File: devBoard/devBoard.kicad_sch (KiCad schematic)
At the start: 1 part, among them U1 ESP32-S3-MINI-1

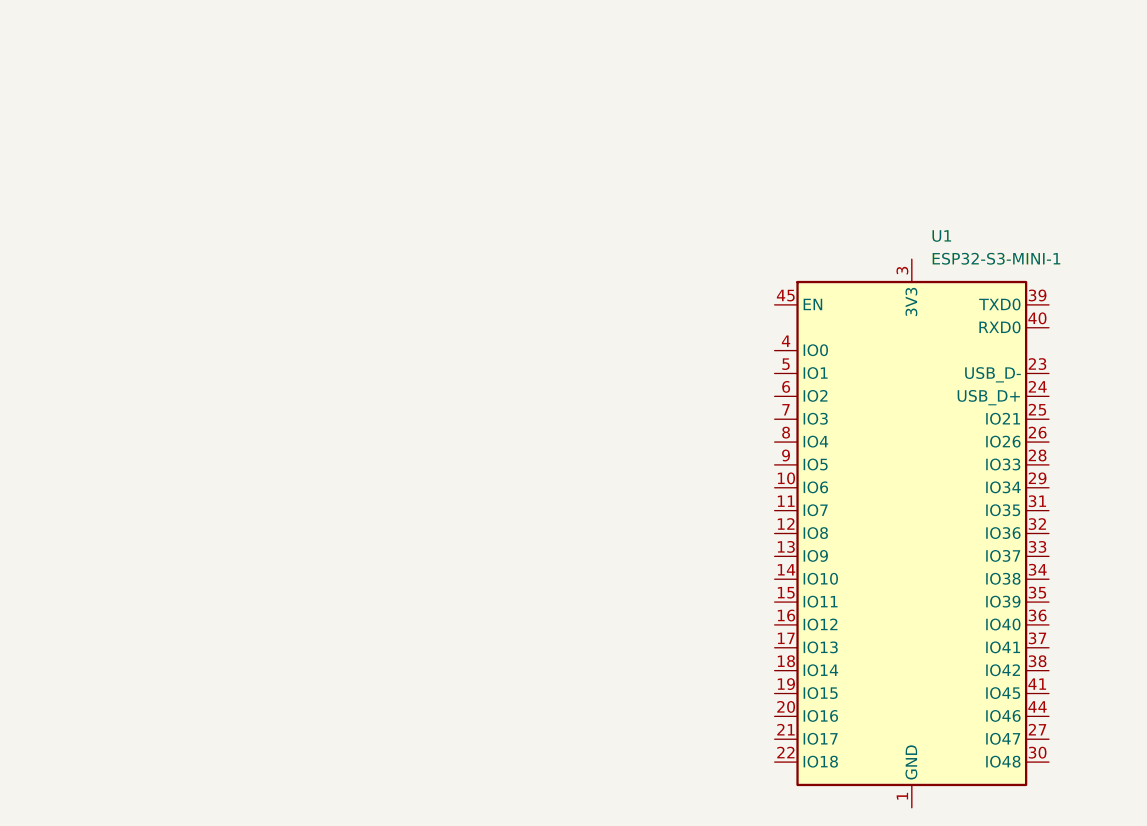
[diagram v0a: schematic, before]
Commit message: IDK why KiCAD changed this file
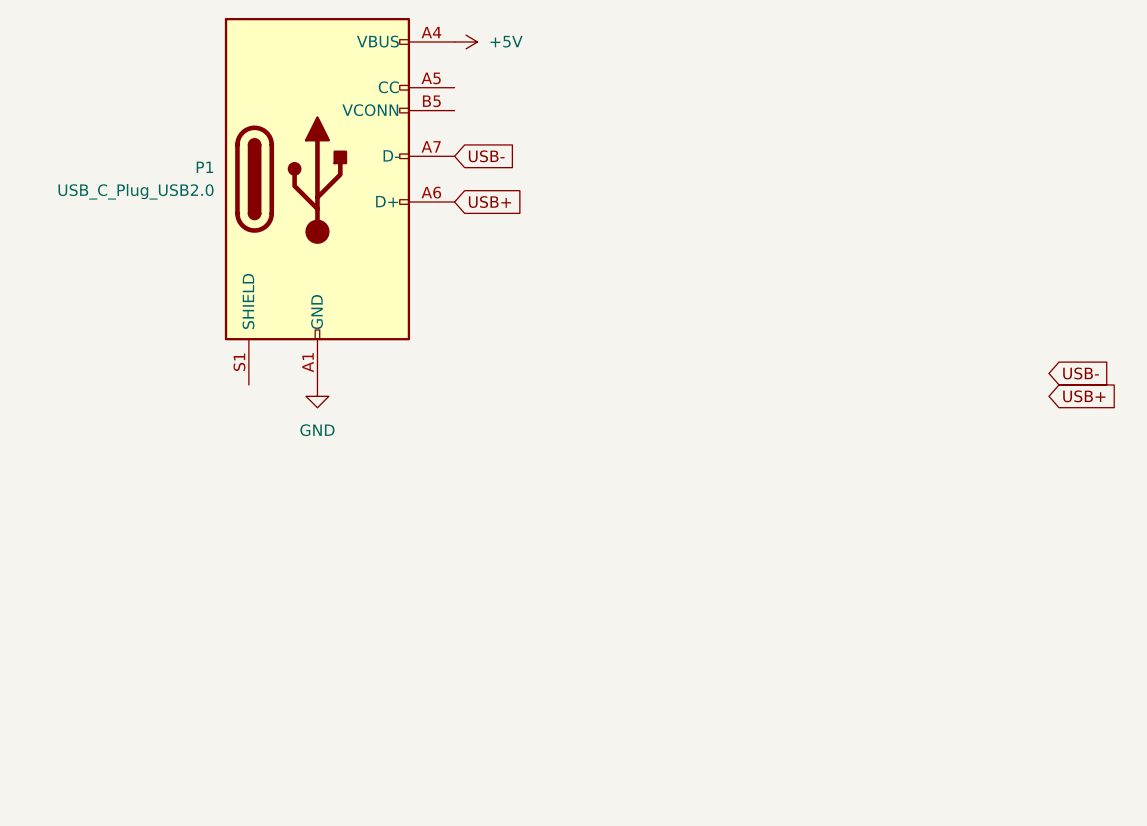
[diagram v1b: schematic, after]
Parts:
- removed U1: ESP32-S3-MINI-1, RF_Module:ESP32-S2-MINI-1, symbol RF_Module:ESP32-S3-MINI-1
- added P1: USB_C_Plug_USB2.0, symbol Connector:USB_C_Plug_USB2.0
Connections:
- new net +5V: P1.A4 (VBUS), P1.A9 (VBUS), P1.B4 (VBUS), P1.B9 (VBUS)
- new net GND: P1.A1 (GND), P1.A12 (GND), P1.B1 (GND), P1.B12 (GND)
- new net USB+: P1.A6 (D+)
- new net USB-: P1.A7 (D-)
